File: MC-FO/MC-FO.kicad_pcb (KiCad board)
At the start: 4 copper layers, 160 x 100 mm, 102 parts, among them J1 86094327313755E1LF, U101 74ACT08SCX, U102 IFE98, U121 74ACT08SCX, U122 IFE98, U141 IFD97, U142 TLV3501AID, U143 74LVC1G32SE-7, U144 74LVC1G0832DBVT, U161 IFD97, U163 74LVC1G32SE-7, U164 74LVC1G0832DBVT, U181 TPS3703A5330DSER, U182 74ACT08SCX, U183 TPS3703A5500DSER, U184 74LVC1G07QDCKTQ1, U2 R-78E3.3-0.5, U27 74ACT08SCX, U28 IFE98, U3 R-78E5.0-0.5, U41 74ACT08SCX, U42 IFE98, U61 74ACT08SCX, U62 IFE98, U81 74ACT08SCX, U82 IFE98

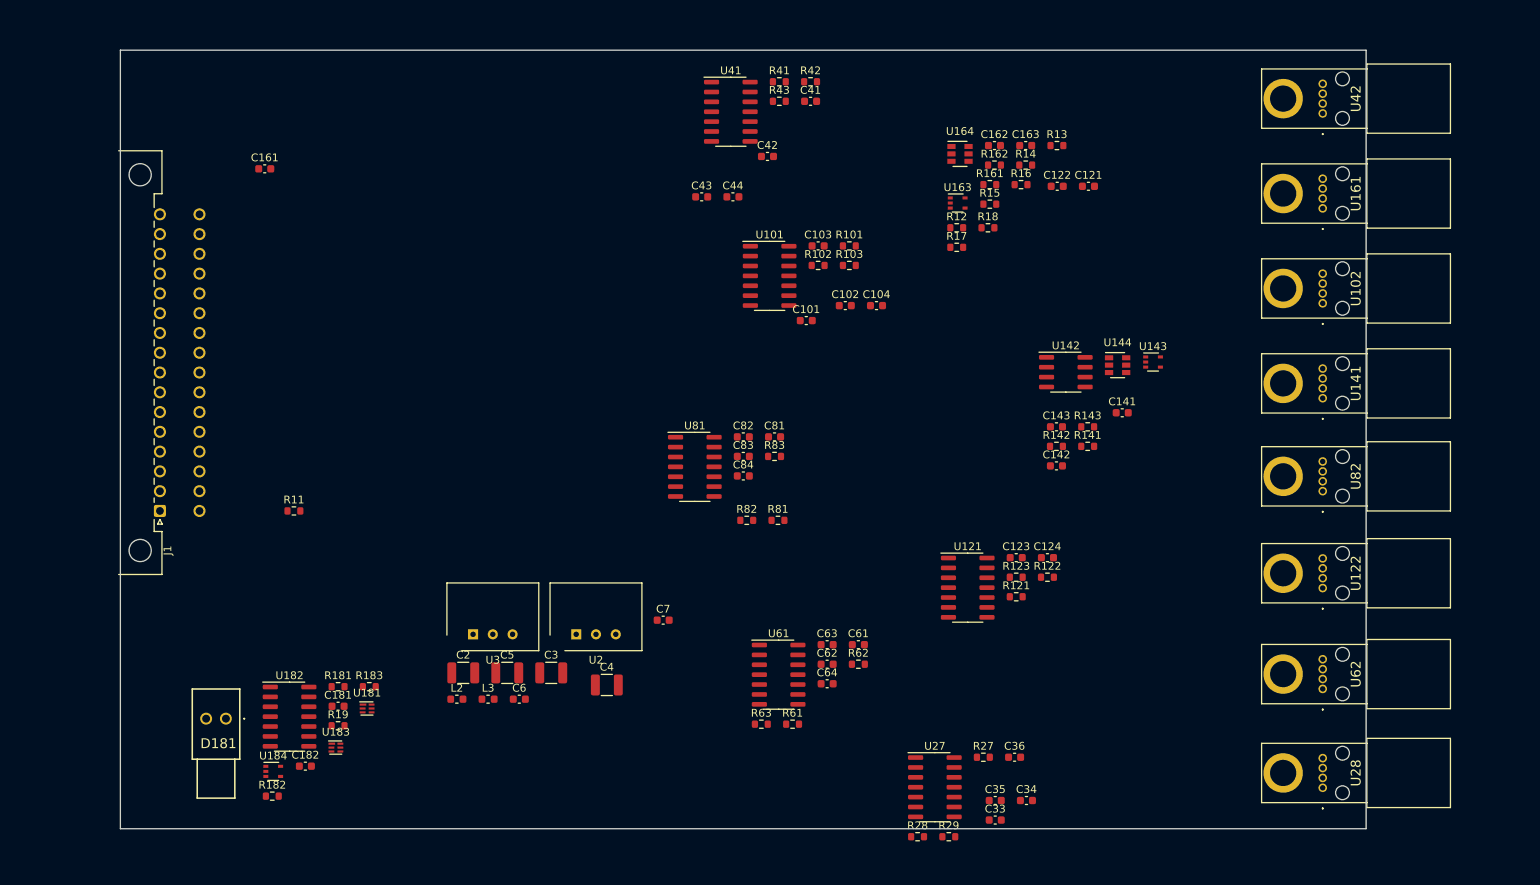
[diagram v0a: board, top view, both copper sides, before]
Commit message: routing prep/organization
moving detectors/emitters around to find where to put status  LED
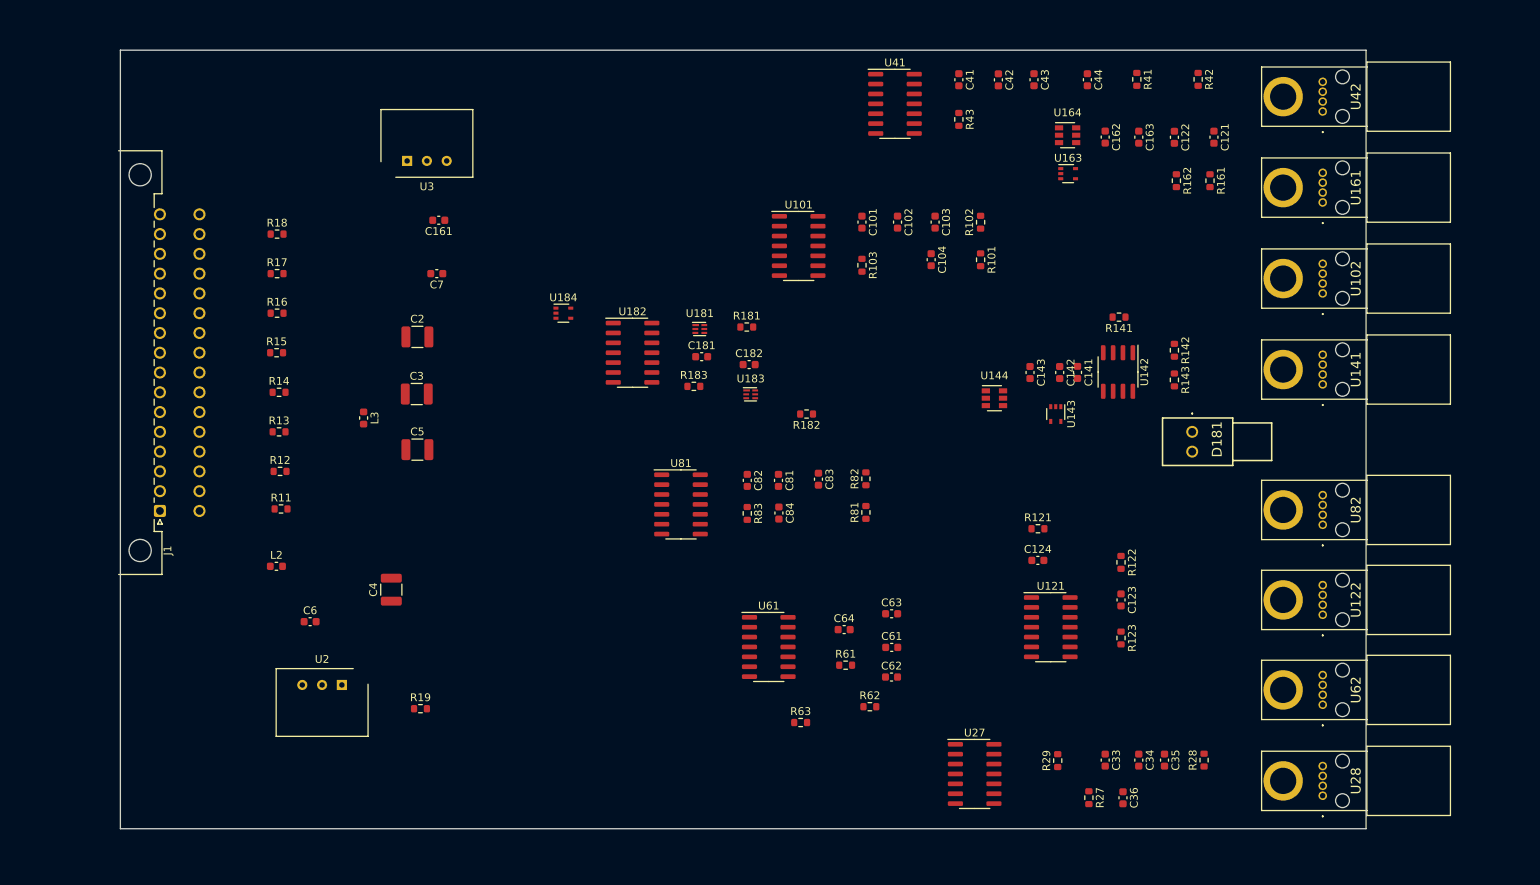
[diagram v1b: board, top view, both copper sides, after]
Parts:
- moved D181 129.5 mm to (224.0, 99.8), turned to 90 degrees
- moved R13 106.5 mm to (106.7, 99.8)
- moved R14 100.2 mm to (106.7, 94.7)
- moved R16 97.0 mm to (106.5, 84.6)
- moved R15 93.6 mm to (106.4, 89.7)
- moved R12 92.4 mm to (106.9, 104.9)
- moved R18 91.3 mm to (106.5, 74.4)
- moved R17 87.4 mm to (106.5, 79.5)
- moved R182 84.4 mm to (174.5, 97.5), turned to 180 degrees
- moved C182 76.9 mm to (167.1, 91.2)
- moved U183 70.0 mm to (167.3, 95.0)
- moved R181 69.9 mm to (166.8, 86.4)
- moved U184 69.7 mm to (143.3, 84.6)
- moved U181 64.8 mm to (160.8, 86.6)
- moved C181 64.8 mm to (161.0, 90.2)
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
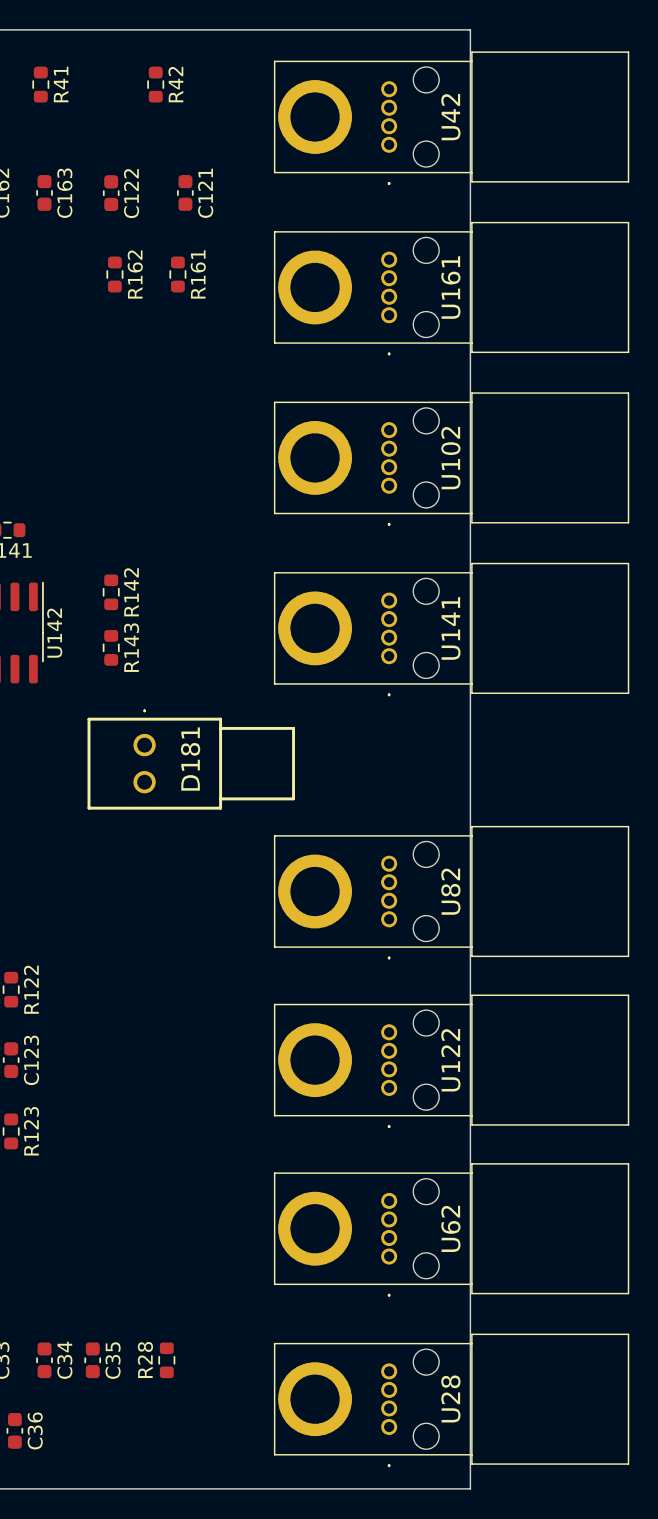
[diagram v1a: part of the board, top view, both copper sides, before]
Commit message: Update LED, Transc. Footprint, layout
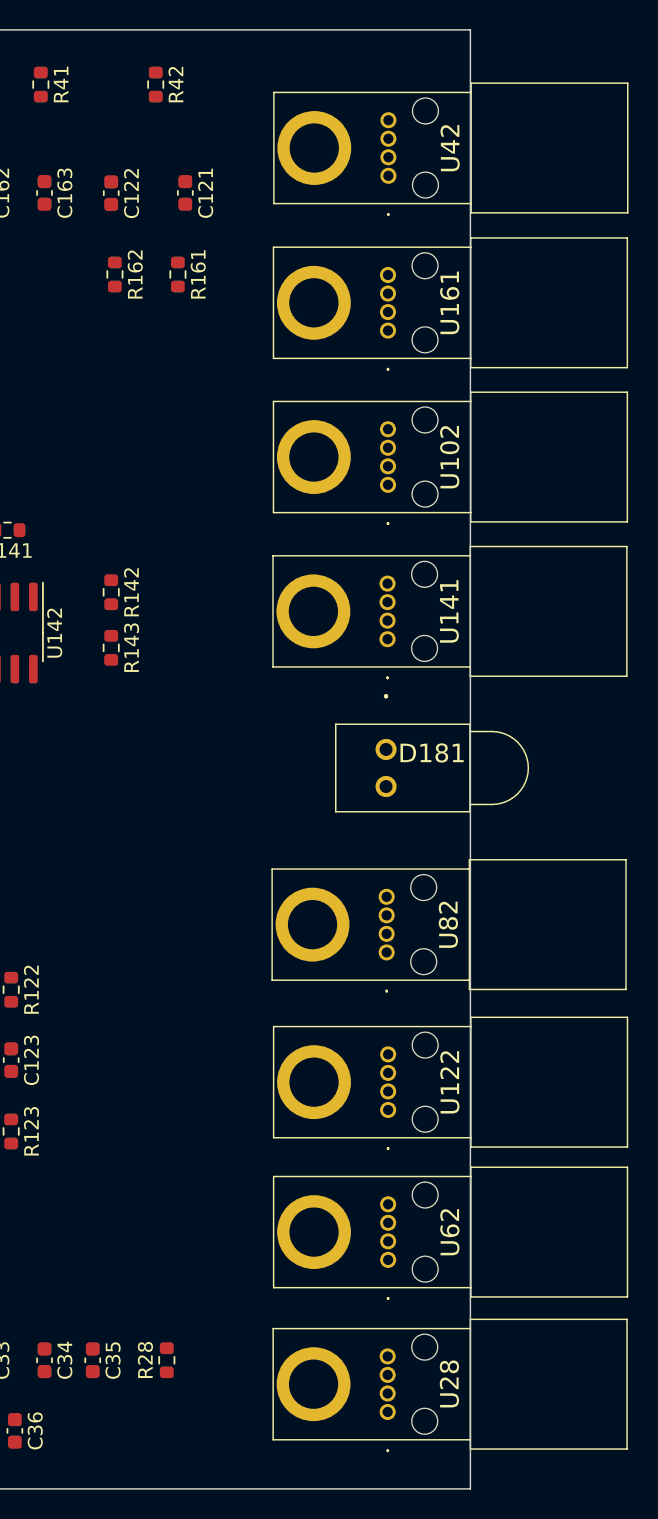
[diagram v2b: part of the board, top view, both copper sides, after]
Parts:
- D181: value 550-2207-004F -> WP1503CB_GD; footprint Footprints_MC-FO:5502207004F -> Footprints_MC-FO:WP1503CBGD
- R161: value 2K -> 2.4K
- R162: value 2K -> 47K
- moved D181 16.6 mm to (240.6, 100.1), turned to 180 degrees
- moved U82 2.28 mm to (240.6, 114.0)
- moved U42 2.13 mm to (240.7, 60.8)
- moved U122 1.51 mm to (240.7, 124.8)
- moved U141 1.17 mm to (240.7, 92.6)
- moved U161 1.06 mm to (240.7, 71.4)
- moved U28 1.03 mm to (240.7, 145.5)
- moved U62 0.24 mm to (240.7, 135.1)
- moved U102 0.10 mm to (240.7, 82.0)

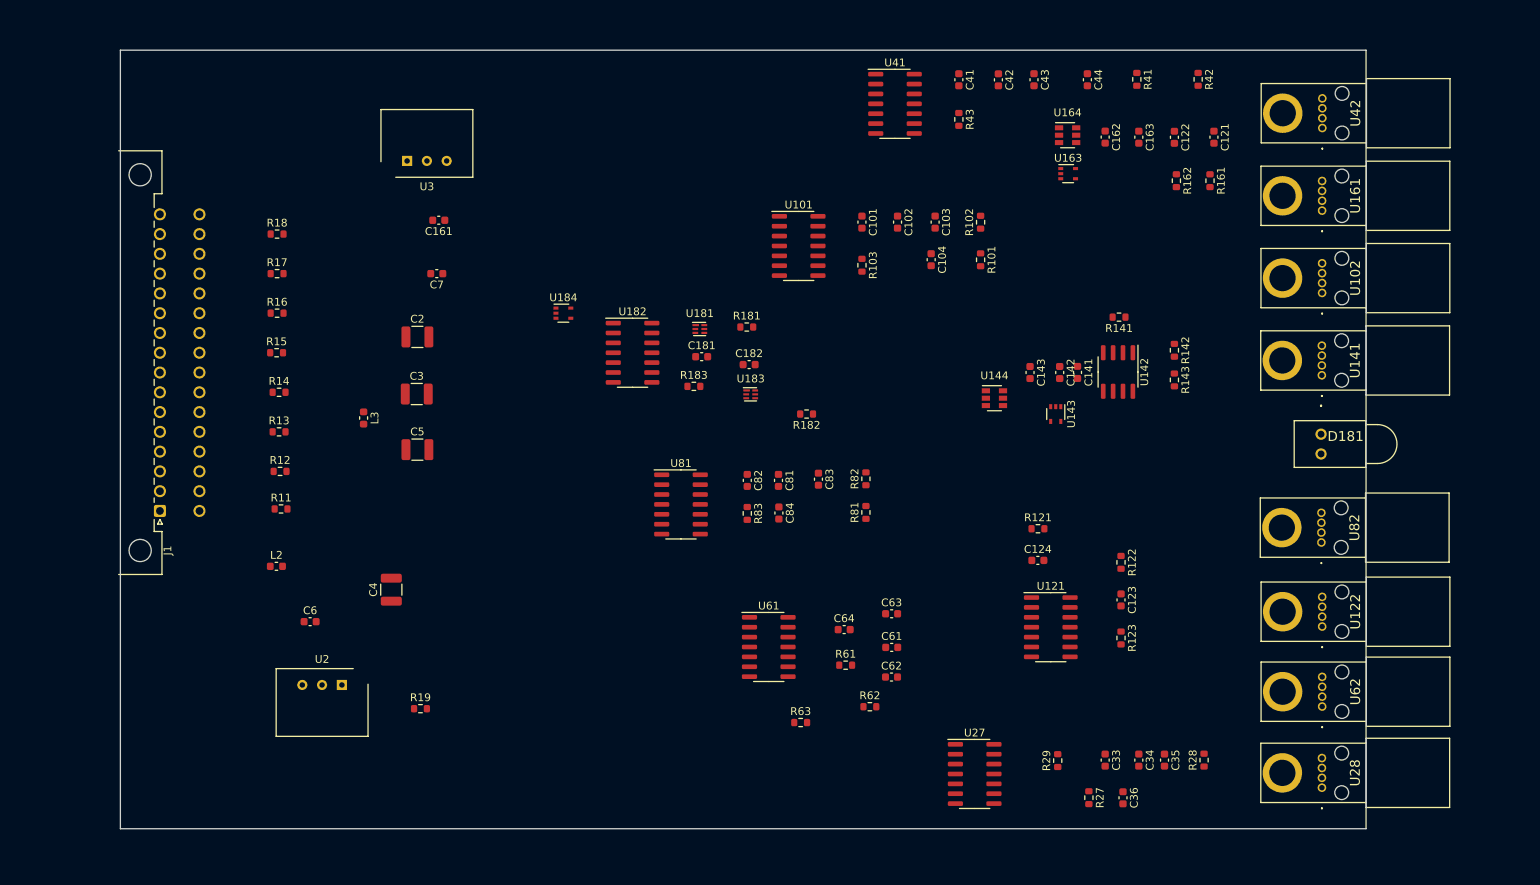
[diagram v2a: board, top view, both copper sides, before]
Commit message: DSP schem, FO schem, and FO layout changes
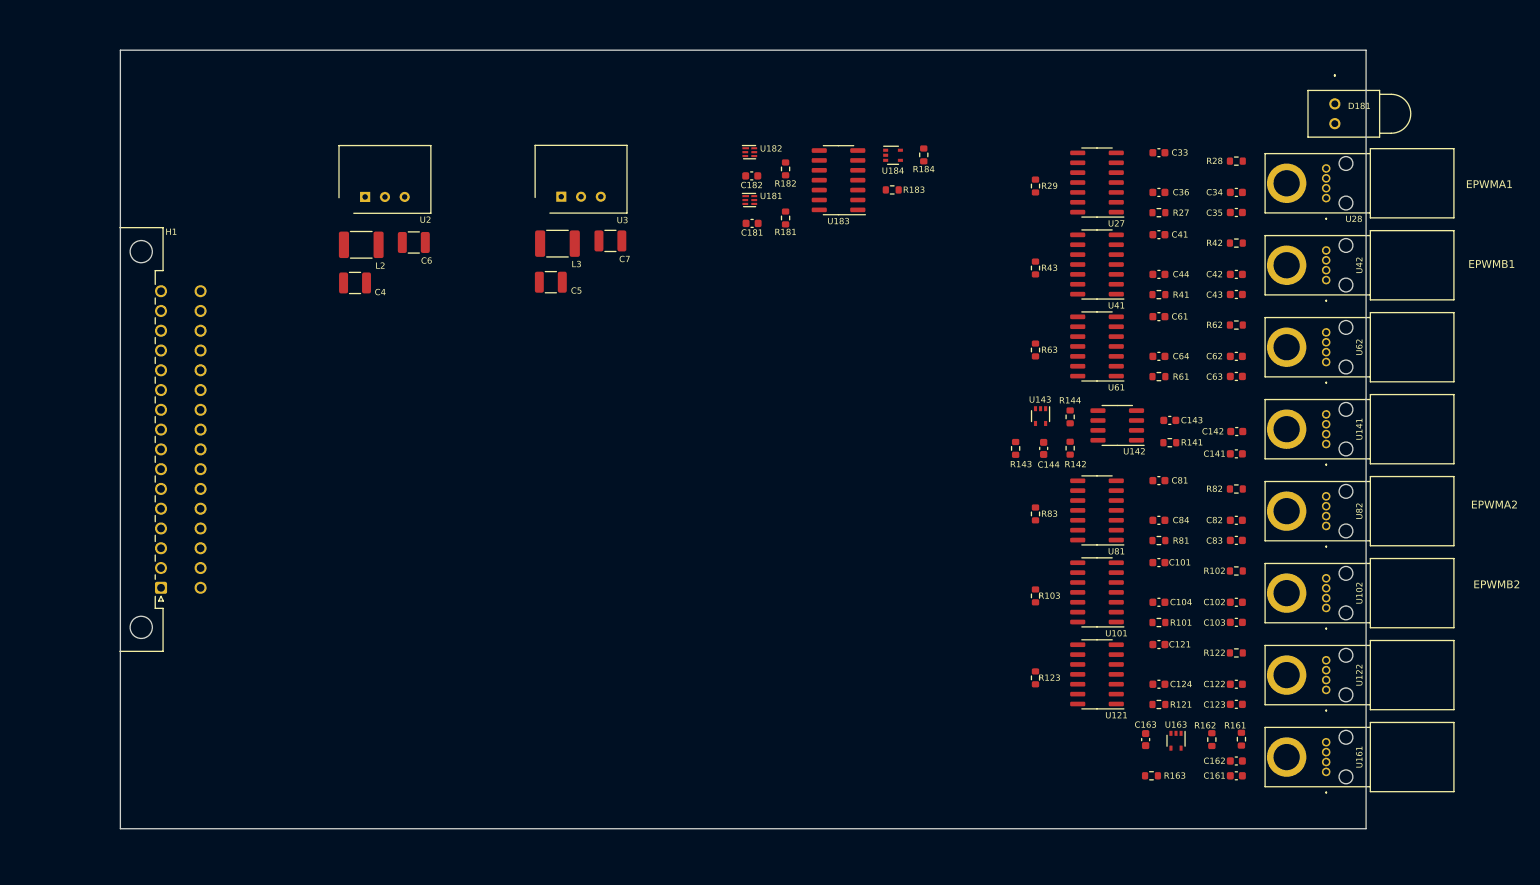
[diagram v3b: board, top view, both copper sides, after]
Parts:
- removed C2, C3: 10 uF, Capacitor_SMD:C_1210_3225Metric
- removed R11, R12, R13, R14, R15, R16, R17: 10K, Resistor_SMD:R_0603_1608Metric
- removed U144, U164: 74LVC1G0832DBVT, Package_TO_SOT_SMD:SOT-23-6
- added C144: 0.1 uF, Capacitor_SMD:C_0603_1608Metric, F.Cu at (204.9, 102.0)
- added R143: 10K, Resistor_SMD:R_0603_1608Metric, F.Cu at (201.3, 102.0)
- C6, C7: footprint Capacitor_SMD:C_0603_1608Metric -> Capacitor_SMD:C_1210_3225Metric
- L2, L3: value 12 uH -> 3.9uH; footprint Inductor_SMD:L_0603_1608Metric -> Inductor_SMD:L_1812_4532Metric_Pad1.30x3.40mm_HandSolder
- R101, R121, R27, R41, R61, R81: value 150 Ohm -> 150R
- R102, R122, R28, R42, R62, R82: value 365 Ohm -> 365R
- R141: value 2.4 K -> 2.4K
- R142: value 1 K -> 1K
- R144: renamed from R143; value 47 K -> 47K
- R181: value 10 K -> 10K
- R182: renamed from R183; value 10 K -> 10K
- R183: renamed from R182; value 500 Ohm -> 500R
- R184: renamed from R19; value 10 K -> 10K
- moved R163 132.1 mm to (218.8, 144.0), turned to 180 degrees
- moved C161 124.8 mm to (229.7, 144.0)
- moved R184 96.1 mm to (189.6, 64.2), turned to 270 degrees
- moved C162 81.9 mm to (229.7, 142.1), turned to 180 degrees
- moved C33 78.3 mm to (219.8, 64.0), turned to 0 degrees
- moved C36 77.9 mm to (219.8, 69.1), turned to 0 degrees
- moved U27 77.6 mm to (211.8, 67.8), turned to 180 degrees
- moved C163 77.4 mm to (218.1, 139.3), turned to 90 degrees
- moved R28 77.0 mm to (229.7, 65.0), turned to 180 degrees
- moved U28 75.7 mm to (241.2, 69.8)
- moved R27 75.7 mm to (219.8, 71.7), turned to 0 degrees
- moved U163 74.1 mm to (221.9, 139.5), turned to 270 degrees
- moved C34 74.0 mm to (229.7, 69.1), turned to 0 degrees
- moved R29 73.9 mm to (203.9, 68.2), turned to 270 degrees
- moved U161 72.1 mm to (241.2, 143.5)
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- renumbered J1 to H1, R18 to R163, U183 to U182, U182 to U183
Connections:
- net /Detector1/RESET_FO renamed /Emitter1/RESET_FO
- C163 pad 1: /Detector1/5V -> VCC
- C4 pad 1: Net-(C4-Pad1) -> 24V
- C5 pad 1: Net-(C5-Pad1) -> 24V
- H1 pad 1: 24V -> GND
- H1 pad 10: Net-(J1-Pad10) -> GND
- H1 pad 11: Net-(J1-Pad11) -> GND
- H1 pad 12: Net-(J1-Pad12) -> GND
- H1 pad 13: Net-(J1-Pad13) -> GND
- H1 pad 14: Net-(J1-Pad14) -> GND
- H1 pad 15: Net-(J1-Pad15) -> GND
- H1 pad 16: GND -> 24V
- H1 pad 17: EPWM1A -> STATUS2
- H1 pad 18: Net-(J1-Pad18) -> GND
- H1 pad 19: EPWM1B -> RESET2
- H1 pad 2: Net-(J1-Pad2) -> GND
- H1 pad 20: Net-(J1-Pad20) -> GND
- H1 pad 21: RESET1 -> EPWM2B
- H1 pad 22: Net-(J1-Pad22) -> GND
- H1 pad 24: Net-(J1-Pad24) -> GND
- H1 pad 25: EPWM2B -> STATUS1
- H1 pad 26: Net-(J1-Pad26) -> GND
- H1 pad 27: RESET2 -> RESET1
- H1 pad 28: Net-(J1-Pad28) -> GND
- H1 pad 29: STATUS1 -> EPWM1B
- H1 pad 3: Net-(J1-Pad3) -> GND
- H1 pad 30: Net-(J1-Pad30) -> GND
- H1 pad 31: STATUS2 -> EPWM1A
- H1 pad 32: Net-(J1-Pad32) -> GND
- H1 pad 4: Net-(J1-Pad4) -> GND
- H1 pad 5: Net-(J1-Pad5) -> GND
- H1 pad 6: Net-(J1-Pad6) -> GND
- H1 pad 7: Net-(J1-Pad7) -> GND
- H1 pad 8: Net-(J1-Pad8) -> GND
- H1 pad 9: Net-(J1-Pad9) -> GND
- L2 pad 2: Net-(C4-Pad1) -> Net-(L2-Pad2)
- L3 pad 2: Net-(C5-Pad1) -> Net-(L3-Pad2)
- R162 pad 1: Net-(R162-Pad1) -> STATUS2
- U143 pad 4: Net-(U143-Pad4) -> STATUS1
- U163 pad 4: Net-(R162-Pad1) -> STATUS2
- U2 pad 1: Net-(C4-Pad1) -> Net-(L2-Pad2)
- U3 pad 1: Net-(C5-Pad1) -> Net-(L3-Pad2)
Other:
- board text added: "EPWMA1"
- board text added: "EPWMA2"
- board text added: "EPWMB1"
- board text added: "EPWMB2"
- board text added: "Reset1"
- board text added: "Reset2"
- board text added: "Status1"
- board text added: "Status2"
